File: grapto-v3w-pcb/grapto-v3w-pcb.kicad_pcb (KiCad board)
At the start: 2 copper layers, 244.5 x 149.5 mm, 214 parts, among them J1 Conn_01x06_Female, J2 USB_C_Receptacle_USB2.0, J3 USB_C_Receptacle_USB2.0, J4 Conn_01x06_Male, J5 Conn_01x06_Female, J6 USB_C_Receptacle_USB2.0, J7 USB_C_Receptacle_USB2.0, J8 Conn_01x06_Male, U1 AP9211S-AL, U11 USBLC6-4SC6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

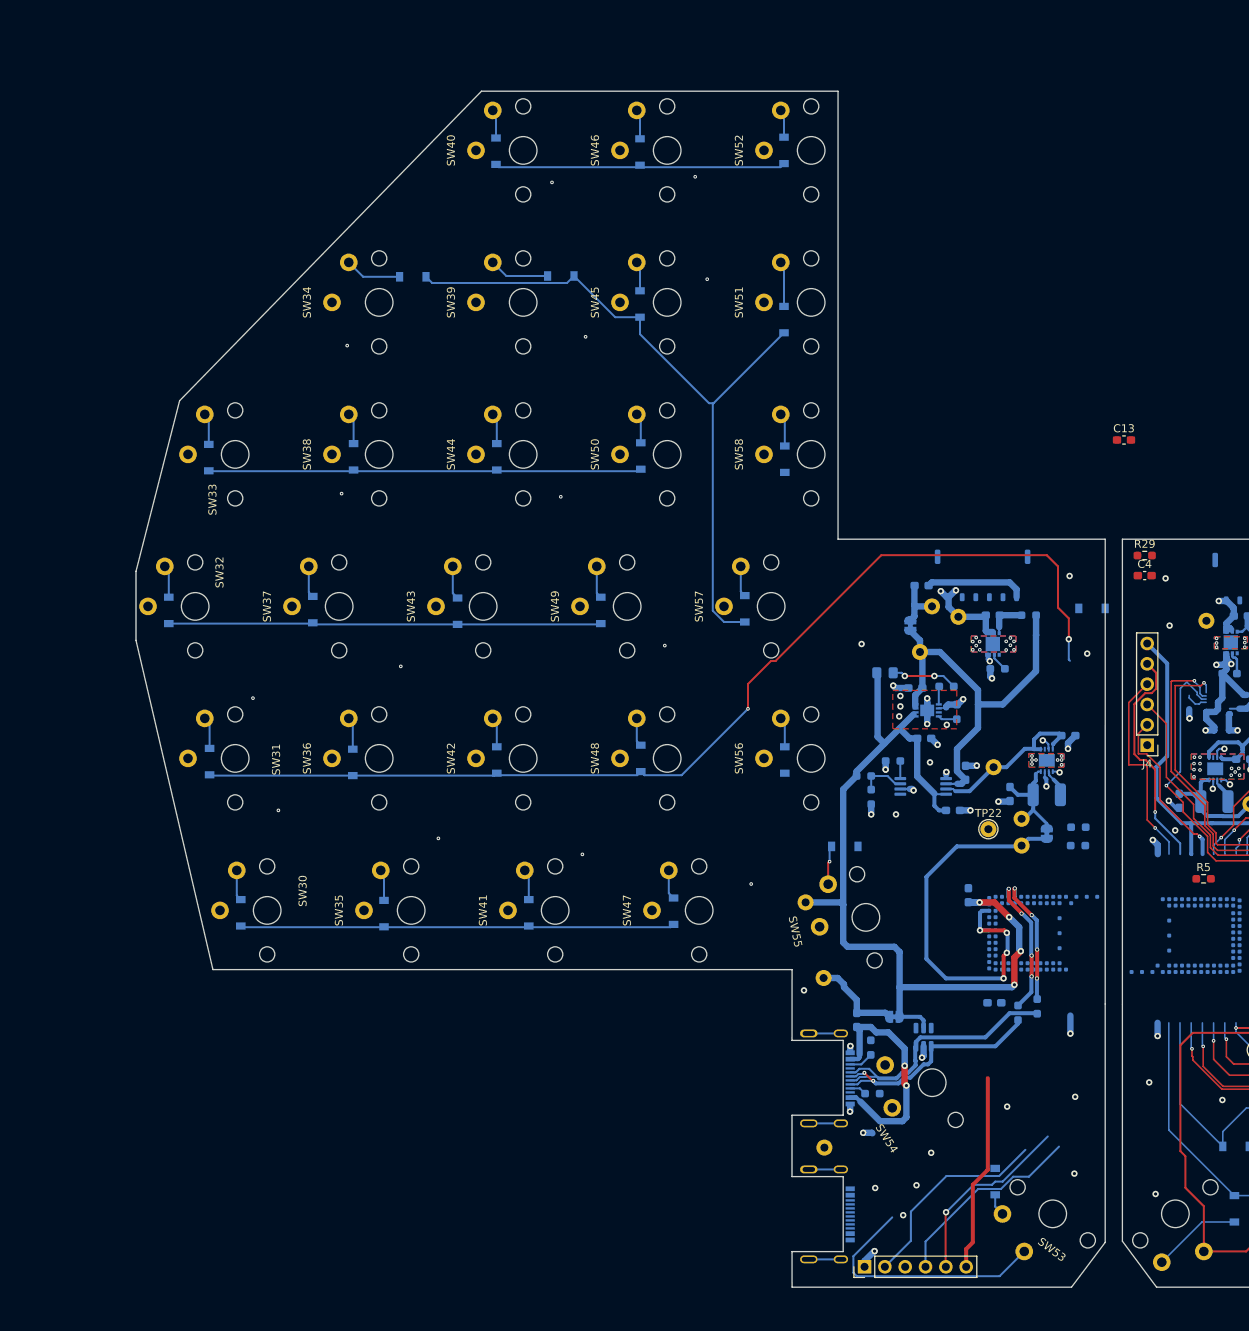
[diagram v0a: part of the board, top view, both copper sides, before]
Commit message: Left half 2 layer initial layout.
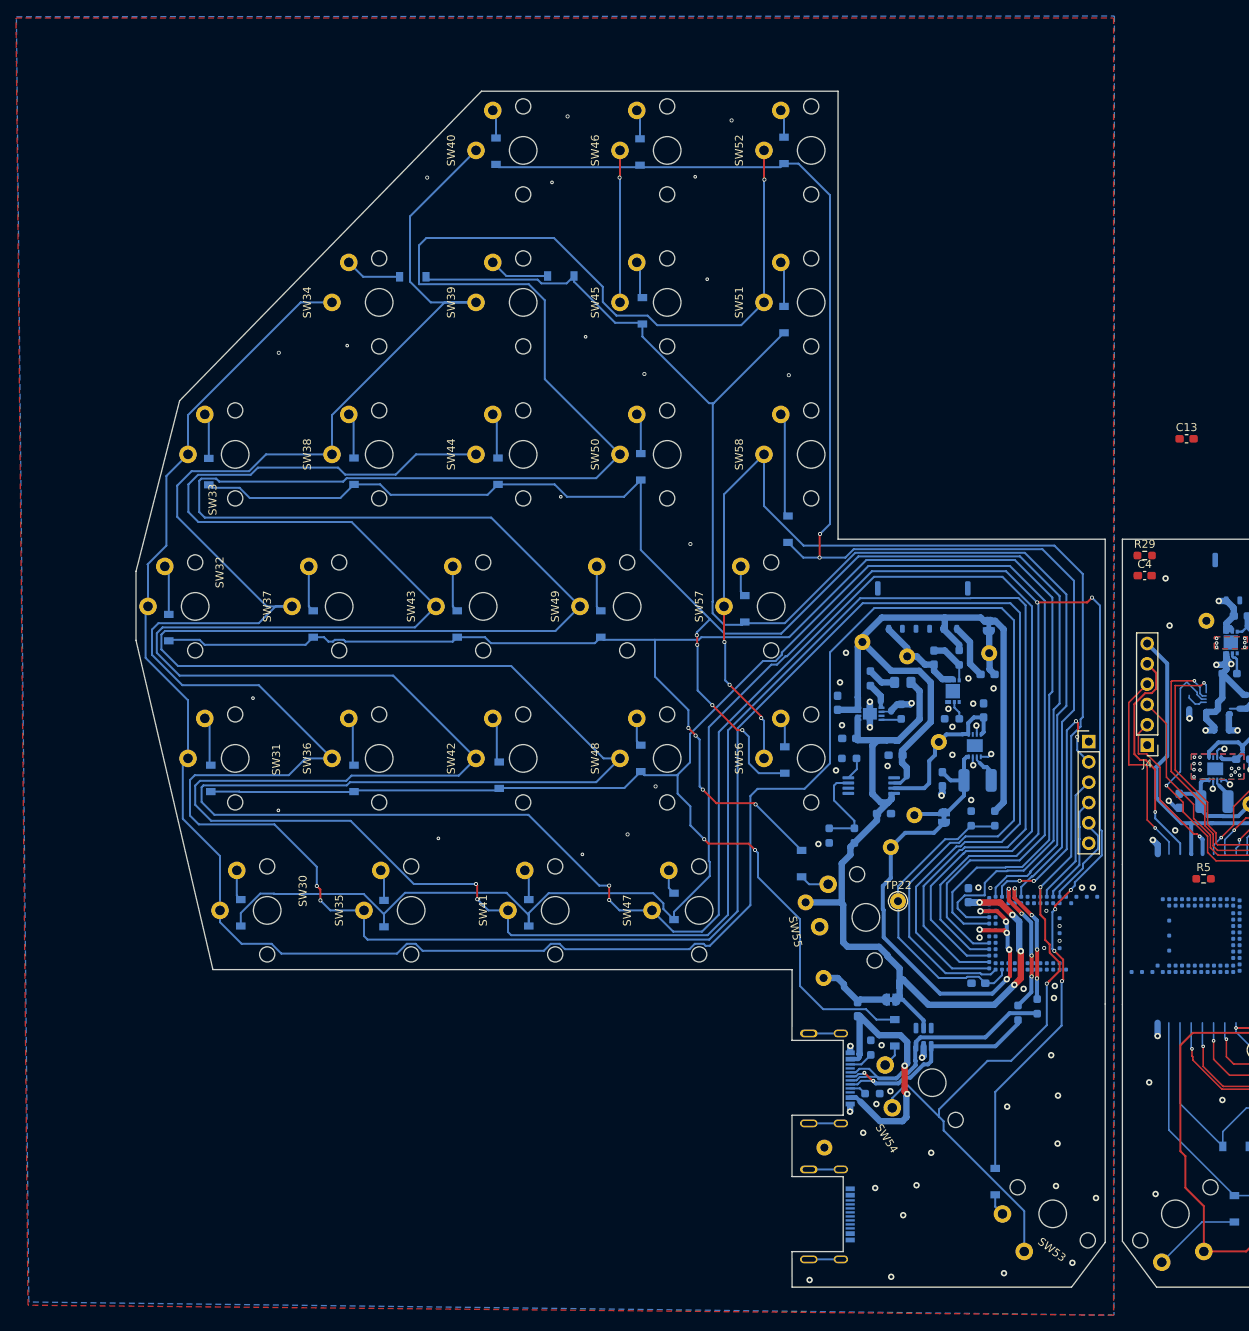
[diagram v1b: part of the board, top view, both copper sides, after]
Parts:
- moved J8 71.4 mm to (175.2, 162.7), turned to 0 degrees
- moved D56 58.5 mm to (150.9, 199.1), turned to 90 degrees
- moved TP18 16.4 mm to (150.4, 175.9)
- moved TP22 14.4 mm to (151.3, 182.7)
- moved F3 13.8 mm to (162.6, 154.3), turned to 0 degrees
- moved R30 13.8 mm to (160.5, 172.3), turned to 90 degrees
- moved TP17 13.4 mm to (153.4, 171.9)
- moved JP6 13.0 mm to (157.1, 172.2)
- moved C16 11.1 mm to (162.1, 158.8), turned to 90 degrees
- moved R19 10.5 mm to (163.4, 172.3), turned to -90 degrees
- moved R15 10.2 mm to (159.0, 152.2), turned to -90 degrees
- moved C12 9.90 mm to (143.8, 157.9), turned to 90 degrees
- moved JP4 9.80 mm to (162.7, 148.3), turned to 90 degrees
- moved R18 9.56 mm to (147.9, 154.8), turned to -90 degrees
- moved C11 9.38 mm to (145.2, 162.3), turned to 180 degrees
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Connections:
- J1 pad 5: unconnected-(J1-Pad5) -> /Right/p+
- J4 pad 6: /Right/3.3v -> unconnected-(J4-Pad6)
- J5 pad 5: unconnected-(J5-Pad5) -> /Left/p+
- J8 pad 6: /Left/3.3v -> unconnected-(J8-Pad6)
- U15 pad 11: /Right/col1 -> unconnected-(U15-Pad11)
- U15 pad 12: unconnected-(U15-Pad12) -> /Right/sysgnd
- U15 pad 13: /Right/col2 -> /Right/col5
- U15 pad 2: unconnected-(U15-Pad2) -> /Right/sysgnd
- U15 pad 21: /Right/col3 -> /Right/col4
- U15 pad 27: /Right/col4 -> /Right/col3
- U15 pad 28: unconnected-(U15-Pad28) -> /Right/sysgnd
- U15 pad 29: /Right/col5 -> /Right/col2
- U15 pad 30: unconnected-(U15-Pad30) -> /Right/sysgnd
- U15 pad 32: unconnected-(U15-Pad32) -> /Right/sysgnd
- U15 pad 35: /Right/row0 -> /Right/col1
- U15 pad 37: /Right/row1 -> /Right/col0
- U15 pad 38: unconnected-(U15-Pad38) -> /Right/sysgnd
- U15 pad 39: /Right/row2 -> /Right/row3
- U15 pad 41: /Right/row3 -> /Right/row2
- U15 pad 42: /Right/low_batt -> /Right/row1
- U15 pad 43: /Right/sysgnd -> /Right/row0
- U15 pad 44: unconnected-(U15-Pad44) -> /Right/sysgnd
- U15 pad 45: /Right/sysgnd -> /Right/low_batt
- U15 pad 50: unconnected-(U15-Pad50) -> /Right/sysgnd
- U15 pad 51: unconnected-(U15-Pad51) -> /Right/sysgnd
- U15 pad 62: unconnected-(U15-Pad62) -> /Right/sysgnd
- U15 pad 63: unconnected-(U15-Pad63) -> /Right/sysgnd
- U15 pad 64: unconnected-(U15-Pad64) -> /Right/sysgnd
- U15 pad 8: unconnected-(U15-Pad8) -> /Right/sysgnd
- U15 pad 9: /Right/col0 -> unconnected-(U15-Pad9)
- U16 pad 11: /Left/col1 -> unconnected-(U16-Pad11)
- U16 pad 12: unconnected-(U16-Pad12) -> /Left/sysgnd
- U16 pad 13: /Left/col2 -> /Left/col5
- U16 pad 2: unconnected-(U16-Pad2) -> /Left/sysgnd
- U16 pad 21: /Left/col3 -> /Left/col4
- U16 pad 27: /Left/col4 -> /Left/col3
- U16 pad 28: unconnected-(U16-Pad28) -> /Left/sysgnd
- U16 pad 29: /Left/col5 -> /Left/col2
- U16 pad 30: unconnected-(U16-Pad30) -> /Left/sysgnd
- U16 pad 32: unconnected-(U16-Pad32) -> /Left/sysgnd
- U16 pad 35: /Left/row0 -> /Left/col1
- U16 pad 37: /Left/row1 -> /Left/col0
- U16 pad 38: unconnected-(U16-Pad38) -> /Left/sysgnd
- U16 pad 39: /Left/row2 -> /Left/row3
- U16 pad 41: /Left/row3 -> /Left/row2
- U16 pad 42: /Left/low_batt -> /Left/row1
- U16 pad 43: /Left/sysgnd -> /Left/row0
- U16 pad 44: unconnected-(U16-Pad44) -> /Left/sysgnd
- U16 pad 45: /Left/sysgnd -> /Left/low_batt
- U16 pad 50: unconnected-(U16-Pad50) -> /Left/sysgnd
- U16 pad 51: unconnected-(U16-Pad51) -> /Left/sysgnd
- U16 pad 62: unconnected-(U16-Pad62) -> /Left/sysgnd
- U16 pad 63: unconnected-(U16-Pad63) -> /Left/sysgnd
- U16 pad 64: unconnected-(U16-Pad64) -> /Left/sysgnd
- U16 pad 8: unconnected-(U16-Pad8) -> /Left/sysgnd
- U16 pad 9: /Left/col0 -> unconnected-(U16-Pad9)
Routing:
- net /Left/row3: track 0.00 -> 600.6 mm, vias 0 -> 3
- net /Left/row2: track 0.00 -> 422.8 mm, vias 0 -> 3
- net /Left/row1: track 0.00 -> 379.7 mm, vias 0 -> 2
- net /Left/row0: track 0.00 -> 291.9 mm
- net /Left/col0: track 54.5 -> 287.2 mm, vias 0 -> 6
- net /Left/row4: track 31.8 -> 202.7 mm, vias 0 -> 5
- net /Left/col2: track 54.2 -> 208.3 mm, vias 0 -> 4
- net /Left/col3: track 54.4 -> 208.4 mm, vias 0 -> 4
- net /Left/col5: track 36.5 -> 170.7 mm, vias 0 -> 2
- net /Left/col1: track 132.9 -> 224.6 mm
- net /Left/col4: track 87.5 -> 177.1 mm
- net /Left/low_batt: track 0.00 -> 38.3 mm
- net /Left/p+: track 51.0 -> 85.4 mm
- net /Left/sysgnd: track 38.2 -> 17.2 mm, vias 55 -> 72
- net /Left/3.3v: track 76.7 -> 56.0 mm, vias 4 -> 6
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- added copper zone on B.Cu, net /Left/sysgnd
- removed copper zone on B.Cu, net /Left/chassi
- removed copper zone on F.Cu, net /Left/chassi

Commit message: Initial 2 layer layout right.
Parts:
- C13, C4, R29, R5: moved to B.Cu
- moved C13 66.6 mm to (197.6, 190.7)
- moved J4 45.5 mm to (182.1, 208.7)
- moved R29 42.3 mm to (200.0, 177.8), turned to -90 degrees
- moved C4 40.2 mm to (195.9, 179.7)
- moved R11 26.0 mm to (190.1, 195.3), turned to 90 degrees
- moved TP5 24.0 mm to (201.5, 195.9)
- moved R10 23.0 mm to (192.9, 195.3), turned to 90 degrees
- moved TP19 18.7 mm to (197.7, 182.7)
- moved TP9 16.6 mm to (200.3, 187.0)
- moved JP3 13.5 mm to (201.1, 183.8), turned to 180 degrees
- moved TP8 9.69 mm to (203.2, 176.3)
- moved D27 9.51 mm to (228.6, 161.9), turned to 0 degrees
- moved C8 9.13 mm to (195.1, 173.3), turned to 90 degrees
- moved L1 9.00 mm to (199.4, 173.2)
- moved U7 8.77 mm to (199.5, 168.3)
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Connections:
- U15 pad 32: /Right/sysgnd -> /Right/3.3v
- U15 pad 34: unconnected-(U15-Pad34) -> /Right/sysgnd
- U15 pad 36: unconnected-(U15-Pad36) -> /Right/col1
- U15 pad 43: /Right/row0 -> /Right/sysgnd
- U15 pad 46: /Right/sysgnd -> /Right/row0
- U16 pad 32: /Left/sysgnd -> /Left/3.3v
- U16 pad 34: unconnected-(U16-Pad34) -> /Left/sysgnd
- U16 pad 36: unconnected-(U16-Pad36) -> /Left/col1
- U16 pad 43: /Left/row0 -> /Left/sysgnd
- U16 pad 46: /Left/sysgnd -> /Left/row0
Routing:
- net /Right/row3: track 169.8 -> 512.9 mm, vias 3 -> 8
- net /Right/row2: track 182.0 -> 471.4 mm, vias 3 -> 5
- net /Right/row1: track 201.9 -> 364.4 mm, vias 2 -> 4
- net (no net): track 126.7 -> 0.00 mm, vias 2 -> 0
- net /Right/col2: track 166.1 -> 292.7 mm, vias 2 -> 6
- net /Right/col0: track 145.2 -> 220.0 mm, vias 2 -> 7
- net /Right/row0: track 204.4 -> 276.2 mm, vias 1 -> 2
- net /Right/3.3v: track 83.3 -> 14.5 mm, vias 2 -> 0
- net /Left/row2: track 422.8 -> 486.4 mm
- net /Right/low_batt: track 71.1 -> 15.2 mm, vias 2 -> 0
- net /Right/col1: track 155.5 -> 207.3 mm, vias 2 -> 5
- net /Right/row4: track 197.0 -> 248.1 mm, vias 3 -> 10
- net /Left/row4: track 202.7 -> 233.6 mm, vias 5 -> 7
- net /Right/status: track 40.5 -> 15.3 mm, vias 1 -> 0
- net /Right/usb1_n: track 49.4 -> 26.7 mm, vias 2 -> 0
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- added copper zone on B.Cu, net /Right/sysgnd

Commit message: Before drc fixes.
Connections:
- U8 pad 7: (no net) -> /Left/chassi
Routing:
- net /Right/sysgnd: track 42.7 -> 42.0 mm
- net /Left/chassi: vias 0 -> 8
- added copper zone on B.Cu, net /Left/chassi
- added copper zone on F.Cu, net /Left/chassi
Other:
- board text removed: "3.3v"

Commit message: 2-layer layout ready to order.
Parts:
- TP1, TP10, TP11, TP12, TP13, TP14, TP15, TP16, TP17, TP18, TP19, TP2, TP22, TP3, TP4, TP5, TP6, TP7, TP8, TP9: footprint TestPoint:TestPoint_THTPad_D2.0mm_Drill1.0mm -> grapto-v3w:TestPoint_THTPad_D2.0mm_Drill1.0mm
- moved JP2 0.48 mm to (204.8, 196.9)
- moved TP7 0.44 mm to (209.6, 162.5)
- moved TP5 0.35 mm to (201.3, 195.7)
- moved TP4 0.33 mm to (208.1, 195.4)
- moved U4 0.33 mm to (202.6, 200.3)
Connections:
- U1 pad 7: (no net) -> /Right/chassi
- U15 pad 59: unconnected-(U15-Pad59) -> /Right/sysgnd
- U16 pad 59: unconnected-(U16-Pad59) -> /Left/sysgnd
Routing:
- net /Right/col2: track 292.7 -> 296.0 mm
- net Net-(C8-Pad1): track 18.0 -> 21.1 mm
- net /Left/row0: track 296.5 -> 294.0 mm
- net /Right/col5: track 184.7 -> 186.5 mm
- net Net-(L1-Pad1): track 4.06 -> 5.51 mm
- net /Right/row4: track 248.1 -> 249.4 mm
- net /Left/row3: track 601.6 -> 602.4 mm
- net /Right/usb1_n: track 26.7 -> 26.0 mm
- net /Left/row2: track 486.4 -> 487.2 mm
- net /Right/col3: track 204.9 -> 205.6 mm
- net /Left/col0: track 275.6 -> 276.2 mm
- net /Left/row1: track 381.6 -> 382.2 mm
- net /Right/usb1_p: track 32.0 -> 31.5 mm
- net /Right/sysgnd: track 42.0 -> 42.5 mm, vias 68 -> 69
- net /Left/sysgnd: track 20.3 -> 20.7 mm, vias 81 -> 80
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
